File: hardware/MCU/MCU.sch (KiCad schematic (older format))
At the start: 31 parts, among them P1 CONN_01X05, P2 CONN_01X04, U1 MAX6369, U2 DS18B20, U4 LM358, Y1 Crystal

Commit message: Especificadas conexiones de las señales DIS y ENA. Actualizado esquematico de la MCU: Actualizadas conexiones, añadido regulador y amplificador
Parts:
- removed C10: 100nF, Capacitors_SMD:C_1206_HandSoldering, symbol C
- removed R5: 4,99K, Resistors_SMD:R_1206_HandSoldering, symbol R
- removed R6: 6,65K, Resistors_SMD:R_1206_HandSoldering, symbol R
- removed U4: LM358, Housings_SOIC:SOIJ-8_5.3x5.3mm_Pitch1.27mm, symbol LM358
- added C11, C12, C13: 100nF, Capacitors_SMD:C_1206_HandSoldering, symbol C
- added C14, C15: 10nF, Capacitors_SMD:C_1206_HandSoldering, symbol C
- added C3: 1uF, symbol C
- added D4, D5: ZENER, symbol ZENER
- added R10, R11, R12, R9: R, symbol R
- added R7: 4,99K, Resistors_SMD:R_1206_HandSoldering, symbol R
- added R8: 6,65K, Resistors_SMD:R_1206_HandSoldering, symbol R
- added U5: LTC6082, symbol LTC6082
- C4: value 10nF -> 1uF; footprint Capacitors_SMD:C_1206_HandSoldering -> (none)
- C6: value 10nF -> 100nF
- R5: renamed from R?; value R -> 4K7
- R6: renamed from R?; value R -> 10K
- gave numbers to parts that had none: 6
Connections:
- net labels added: +BATT, F_RF_IN
- wire segments 122 -> 178
- no-connect marks 30 -> 29
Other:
- note added: "2.7 V"
- note added: "DEV"
- moved on the sheet: C1, C2, C8, C9, P1, P2, P3, U2, U3, Y1

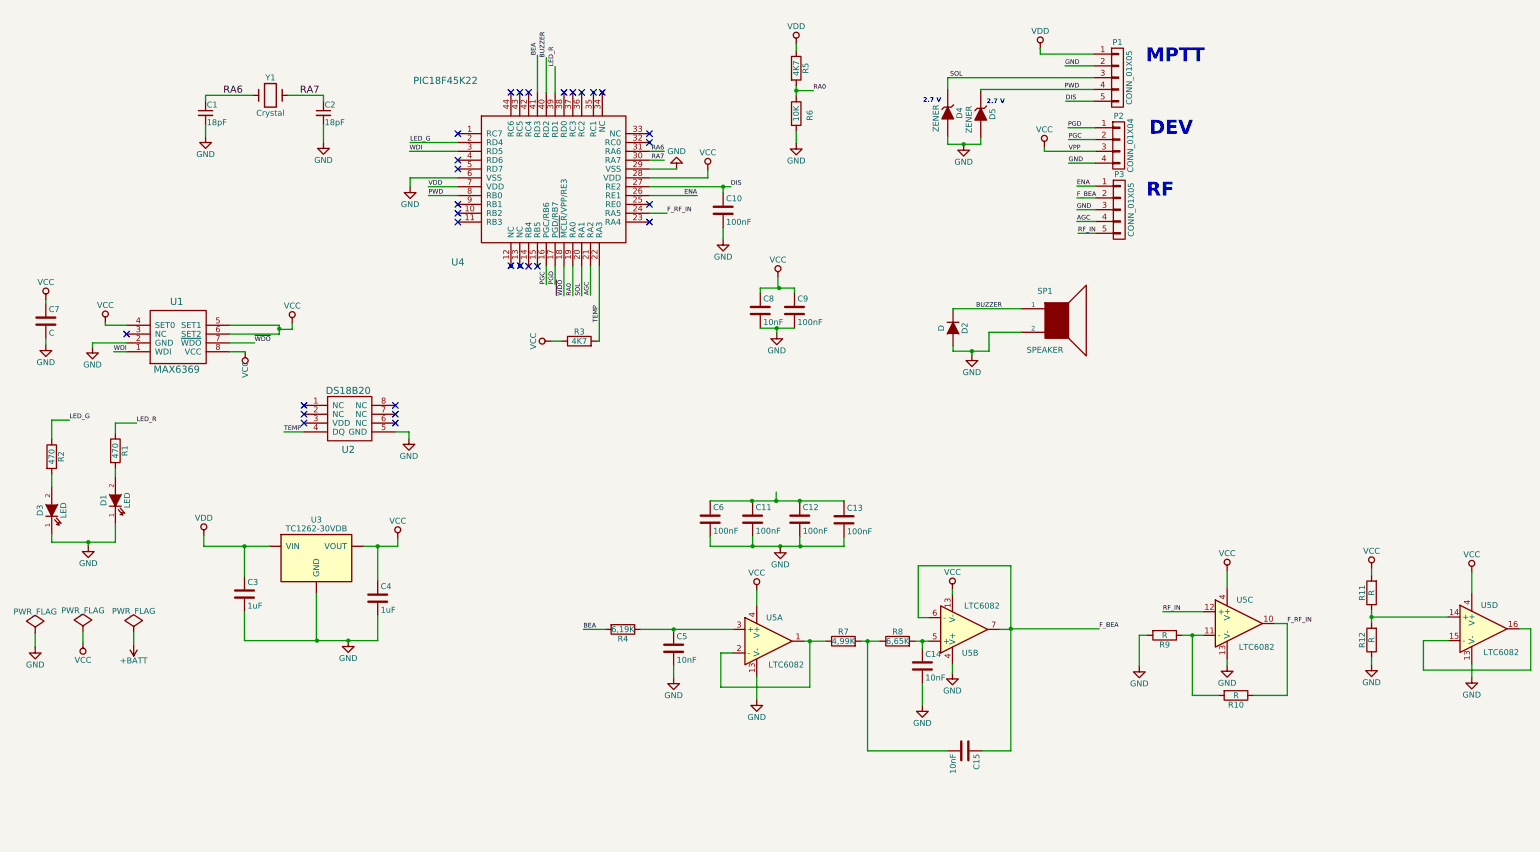
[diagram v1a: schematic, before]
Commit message: Añadida libreria del amplificador operacional LT6005. Añadido a los esquematicos.
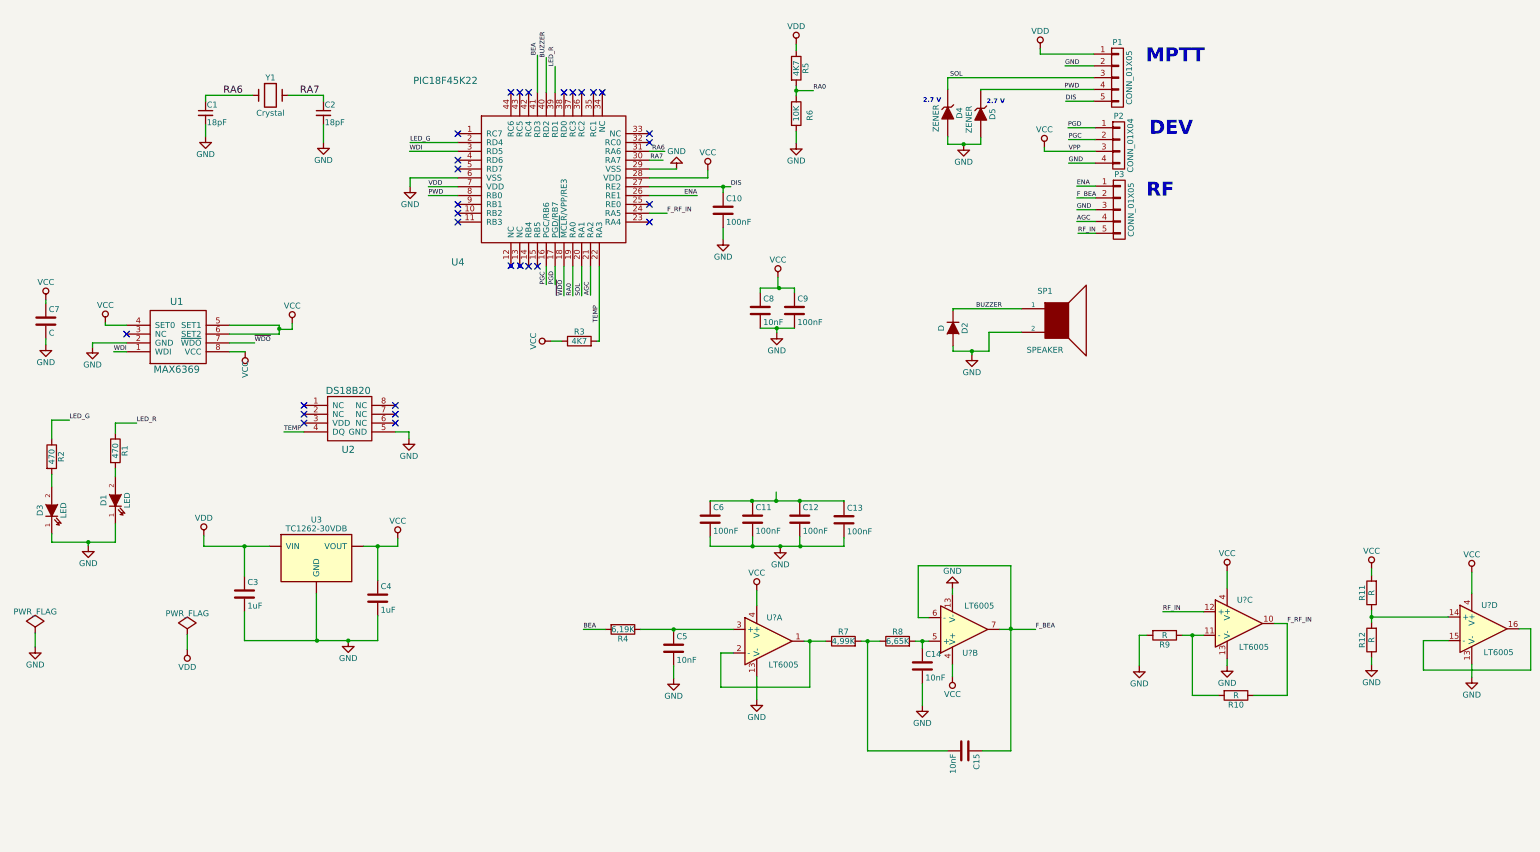
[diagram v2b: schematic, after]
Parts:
- removed U5: LTC6082, symbol LTC6082
- added U? (x4): LT6005, symbol LT6005
- R10, R11, R12, R9: footprint (none) -> Resistors_SMD:R_1206_HandSoldering
- U4: footprint (none) -> Housings_QFP:TQFP-44-1EP_10x10mm_Pitch0.8mm
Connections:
- net F_BEA: now also U?.7
- net F_RF_IN: now also U?.10
- net GND: now also C5.2, U?.13 (V-), U?.13 (V-), U?.13 (V-), U?.13 (V-)
- net RF_IN: now also U?.12 (+)
- net VCC: now also U?.4 (V+), U?.4 (V+), U?.4 (V+), U?.4 (V+)
- net at R7.1: now also U?.1, U?.2 (-)
- net at C5.1, R4.1: now also U?.3 (+)
- net at C14.1, R8.2: now also U?.5 (+)
- net at C15.1: now also U?.6 (-)
- net at R10.2, R9.1: now also U?.11 (-)
- net at R11.1, R12.2: now also U?.14 (+)
- new net: U?.15 (-), U?.16

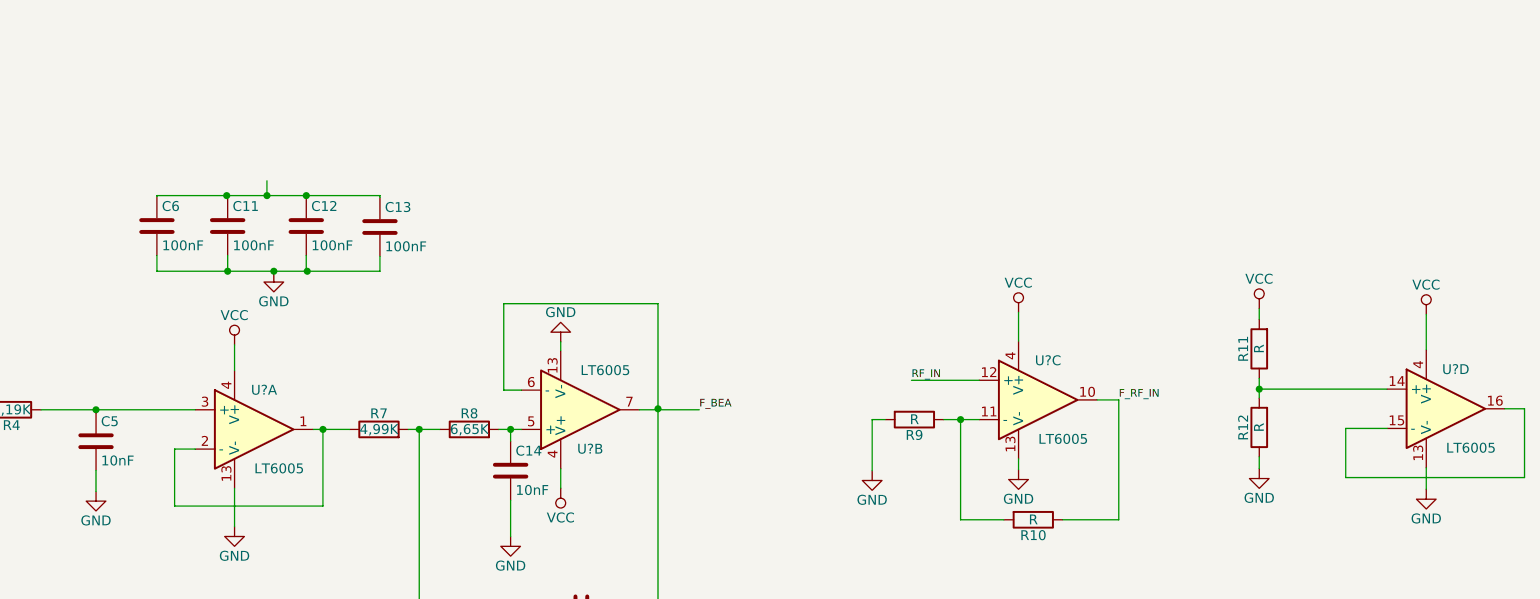
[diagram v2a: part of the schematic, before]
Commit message: Puestas todas las huellas. Primera colocacion de los componentes hecha. A la espera de la revision de los esquematicos para rutar
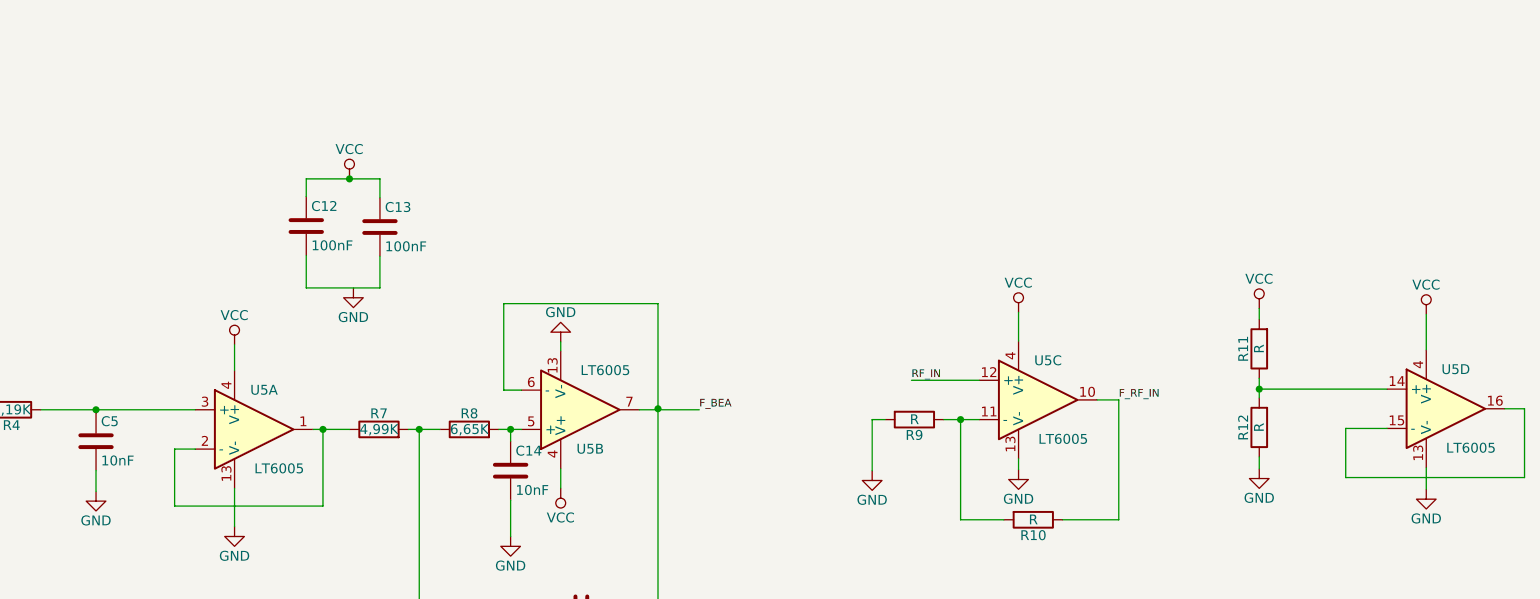
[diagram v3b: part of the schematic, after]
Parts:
- removed C11, C6: 100nF, Capacitors_SMD:C_1206_HandSoldering, symbol C
- C1, C10, C12, C13, C14, C15, C2, C5, C7, C8, C9: footprint Capacitors_SMD:C_1206_HandSoldering -> Capacitors_SMD:C_0603_HandSoldering
- C3, C4: footprint (none) -> Capacitors_SMD:C_0603_HandSoldering
- D3: footprint (none) -> LEDs:LED_1206
- D4, D5: footprint (none) -> Diodes_SMD:D_SOD-123
- P1: footprint Connectors_Terminal_Blocks:TerminalBlock_Pheonix_MPT-2.54mm_5pol -> Sockets_MOLEX_KK-System:Socket_MOLEX-KK-RM2-54mm_Lock_5pin_straight
- P2: footprint Connectors_Terminal_Blocks:TerminalBlock_Pheonix_MPT-2.54mm_4pol -> Sockets_MOLEX_KK-System:Socket_MOLEX-KK-RM2-54mm_Lock_4pin_straight
- P3: footprint Connectors_Terminal_Blocks:TerminalBlock_Pheonix_MPT-2.54mm_5pol -> Sockets_MOLEX_KK-System:Socket_MOLEX-KK-RM2-54mm_Lock_4pin_straight
- R1, R10, R11, R12, R2, R3, R4, R7, R8, R9: footprint Resistors_SMD:R_1206_HandSoldering -> Resistors_SMD:R_0603_HandSoldering
- R5, R6: footprint (none) -> Resistors_SMD:R_0603_HandSoldering
- U4: footprint Housings_QFP:TQFP-44-1EP_10x10mm_Pitch0.8mm -> Housings_QFP:LQFP-44_10x10mm_Pitch0.8mm
- U5: renamed from U?; footprint (none) -> Housings_SSOP:SSOP-16_3.9x4.9mm_Pitch0.635mm
- gave numbers to parts that had none: 1
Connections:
- net GND: no longer C12.2, C13.2
- net VCC: now also C12.1, C13.1
- new net: C12.2, C13.2

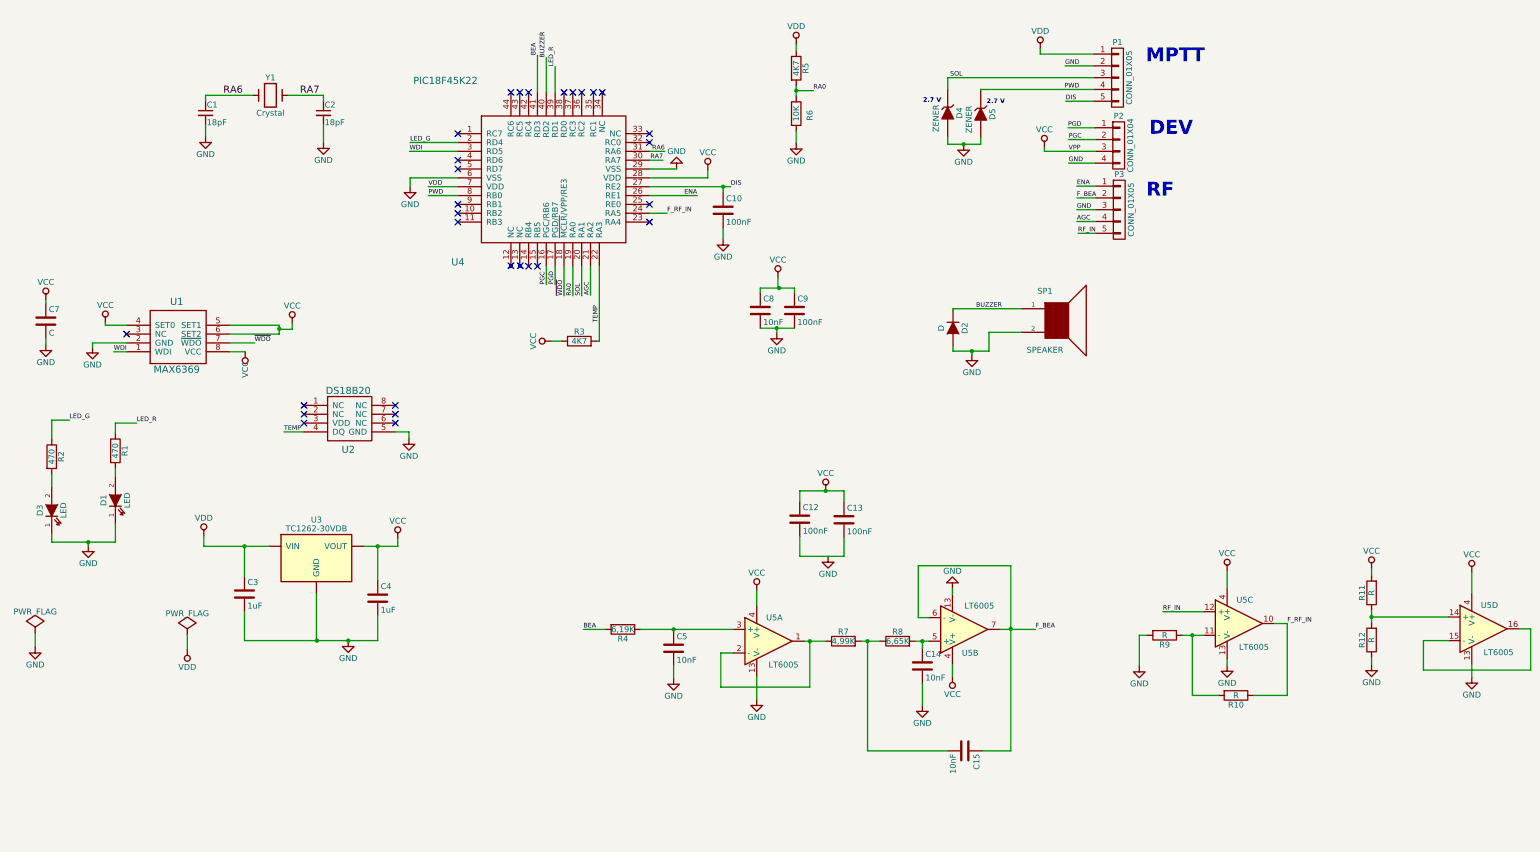
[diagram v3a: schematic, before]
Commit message: Añadidas señales PTT, RPT, HIPWR, BEACON_MODE. Añadido un conector
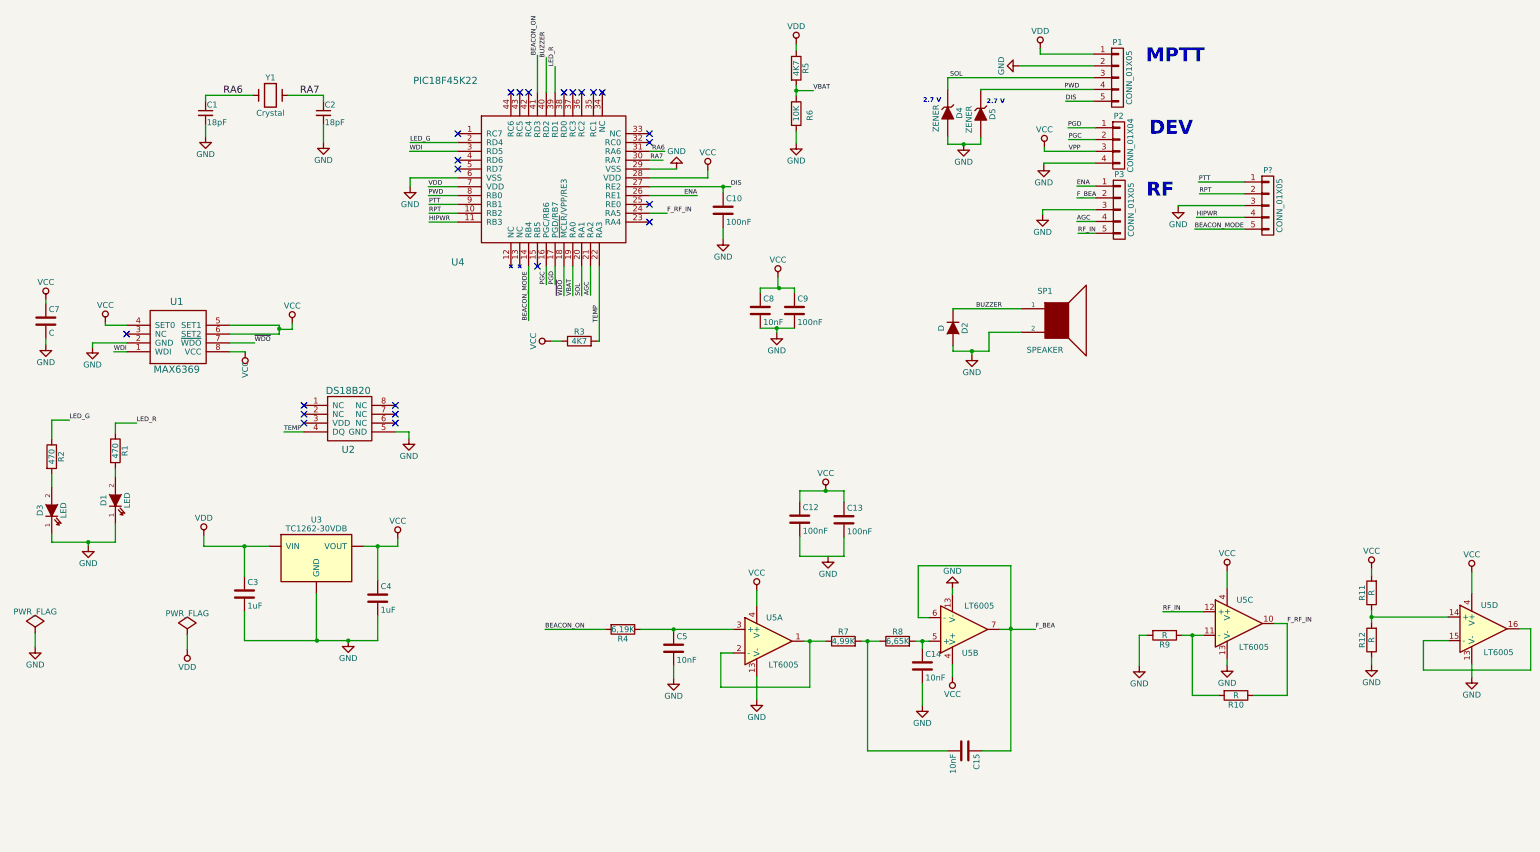
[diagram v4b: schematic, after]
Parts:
- added P?: CONN_01X05, Sockets_MOLEX_KK-System:Socket_MOLEX-KK-RM2-54mm_Lock_4pin_straight, symbol CONN_01X05
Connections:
- net GND: now also P?.3 (P3)
- net RPT: now reaches U4.10 (RB2)
- net RPT: now also P?.2 (P2)
- net HIPWR: now reaches U4.11 (RB3)
- net HIPWR: now also P?.4 (P4)
- net BEACON_MODE: now reaches U4.14 (RB4)
- net BEACON_MODE: now also P?.5 (P5)
- net PTT: now reaches U4.9 (RB1)
- net PTT: now also P?.1 (P1)
- net BEA renamed BEACON_ON
- net RA0 renamed VBAT
- no-connect marks 29 -> 23
